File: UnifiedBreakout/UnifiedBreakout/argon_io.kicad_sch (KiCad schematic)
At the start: 3 parts, among them J14 ARGON J5

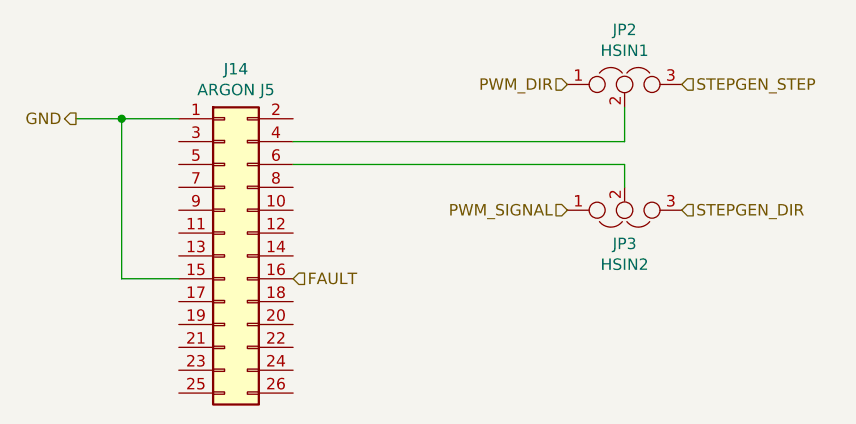
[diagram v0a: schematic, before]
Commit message: Upgrade to new KiCAD version
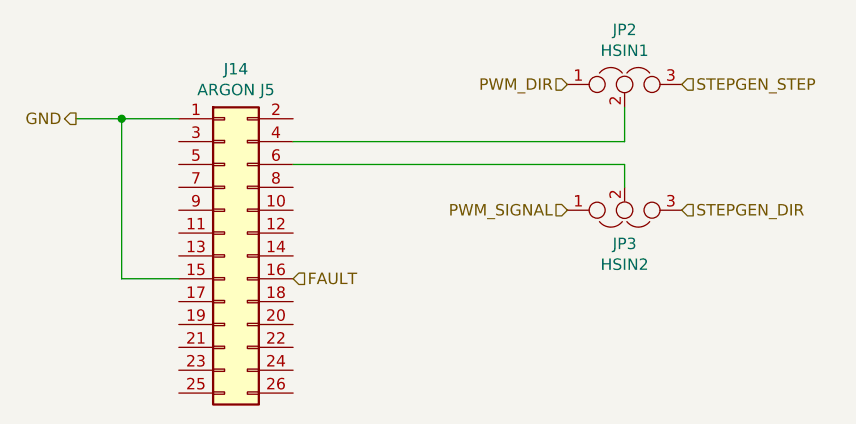
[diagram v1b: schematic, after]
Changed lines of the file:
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@@
-(kicad_sch (version 20210126) (generator eeschema)
+(kicad_sch (version 20211123) (generator eeschema)
   (paper "A4")
-  (junction (at 121.92 76.2) (diameter 0.9144) (color 0 0 0 0))
+  (junction (at 121.92 76.2) (diameter 0.9144) (color 0 0 0 0)
+  )
+  (wire (pts (xy 177.8 74.93) (xy 177.8 78.74))
+    (stroke (width 0) (type solid) (color 0 0 0 0))
+  )
   (wire (pts (xy 121.92 76.2) (xy 116.84 76.2))
     (stroke (width 0) (type solid) (color 0 0 0 0))
   )
+  (wire (pts (xy 140.97 81.28) (xy 177.8 81.28))
+    (stroke (width 0) (type solid) (color 0 0 0 0))
+  )
+  (wire (pts (xy 177.8 81.28) (xy 177.8 83.82))
+    (stroke (width 0) (type solid) (color 0 0 0 0))
+  )
   (wire (pts (xy 121.92 93.98) (xy 121.92 76.2))
+    (stroke (width 0) (type solid) (color 0 0 0 0))
+  )
+  (wire (pts (xy 140.97 78.74) (xy 177.8 78.74))
     (stroke (width 0) (type solid) (color 0 0 0 0))
   )
@@
     (stroke (width 0) (type solid) (color 0 0 0 0))
   )
-  (wire (pts (xy 140.97 78.74) (xy 177.8 78.74))
-    (stroke (width 0) (type solid) (color 0 0 0 0))
-  )
-  (wire (pts (xy 140.97 81.28) (xy 177.8 81.28))
-    (stroke (width 0) (type solid) (color 0 0 0 0))
-  )
-  (wire (pts (xy 177.8 74.93) (xy 177.8 78.74))
-    (stroke (width 0) (type solid) (color 0 0 0 0))
-  )
-  (wire (pts (xy 177.8 81.28) (xy 177.8 83.82))
-    (stroke (width 0) (type solid) (color 0 0 0 0))
-  )
   (hierarchical_label "GND" (shape output) (at 116.84 76.2 180)
-    (effects (font (size 1.27 1.27)) (justify right))
-  )
-  (hierarchical_label "FAULT" (shape input) (at 140.97 93.98 0)
-    (effects (font (size 1.27 1.27)) (justify left))
-  )
-  (hierarchical_label "PWM_DIR" (shape input) (at 171.45 72.39 180)
     (effects (font (size 1.27 1.27)) (justify right))
   )
@@
     (effects (font (size 1.27 1.27)) (justify left))
   )
-  (symbol (lib_id "UnifiedBreakout-rescue:Jumper_NC_Dual-Device") (at 177.8 72.39 0) (unit 1)
-    (in_bom yes) (on_board yes)
-    (property "Reference" "JP2" (id 0) (at 177.8 66.3194 0))
-    (property "Value" "HSIN1" (id 1) (at 177.8 68.6308 0))
-    (property "Footprint" "Connector_PinHeader_2.54mm:PinHeader_1x03_P2.54mm_Vertical" (id 2) (at 177.8 72.39 0)
-      (effects (font (size 1.27 1.27)) hide)
-    )
-    (property "Datasheet" "~" (id 3) (at 177.8 72.39 0)
-      (effects (font (size 1.27 1.27)) hide)
-    )
-    (pin "1")
-    (pin "2")
-    (pin "3")
+  (hierarchical_label "FAULT" (shape input) (at 140.97 93.98 0)
+    (effects (font (size 1.27 1.27)) (justify left))
   )
-  (symbol (lib_id "UnifiedBreakout-rescue:Jumper_NC_Dual-Device") (at 177.8 86.36 0) (mirror x) (unit 1)
-    (in_bom yes) (on_board yes)
-    (property "Reference" "JP3" (id 0) (at 177.8 90.0938 0))
-    (property "Value" "HSIN2" (id 1) (at 177.8 92.4052 0))
-    (property "Footprint" "Connector_PinHeader_2.54mm:PinHeader_1x03_P2.54mm_Vertical" (id 2) (at 177.8 86.36 0)
-      (effects (font (size 1.27 1.27)) hide)
-    )
-    (property "Datasheet" "~" (id 3) (at 177.8 86.36 0)
-      (effects (font (size 1.27 1.27)) hide)
-    )
-    (pin "1")
-    (pin "2")
-    (pin "3")
+  (hierarchical_label "PWM_DIR" (shape input) (at 171.45 72.39 180)
+    (effects (font (size 1.27 1.27)) (justify right))
   )
   (symbol (lib_id "UnifiedBreakout-rescue:Conn_02x13_Odd_Even-Connector_Generic") (at 133.35 91.44 0) (unit 1)
@@
     (pin "9")
   )
+  (symbol (lib_id "UnifiedBreakout-rescue:Jumper_NC_Dual-Device") (at 177.8 72.39 0) (unit 1)
+    (in_bom yes) (on_board yes)
+    (property "Reference" "JP2" (id 0) (at 177.8 66.3194 0))
+    (property "Value" "HSIN1" (id 1) (at 177.8 68.6308 0))
+    (property "Footprint" "Connector_PinHeader_2.54mm:PinHeader_1x03_P2.54mm_Vertical" (id 2) (at 177.8 72.39 0)
+      (effects (font (size 1.27 1.27)) hide)
+    )
+    (property "Datasheet" "~" (id 3) (at 177.8 72.39 0)
+      (effects (font (size 1.27 1.27)) hide)
+    )
+    (pin "1")
+    (pin "2")
+    (pin "3")
+  )
+  (symbol (lib_id "UnifiedBreakout-rescue:Jumper_NC_Dual-Device") (at 177.8 86.36 0) (mirror x) (unit 1)
+    (in_bom yes) (on_board yes)
+    (property "Reference" "JP3" (id 0) (at 177.8 90.0938 0))
+    (property "Value" "HSIN2" (id 1) (at 177.8 92.4052 0))
+    (property "Footprint" "Connector_PinHeader_2.54mm:PinHeader_1x03_P2.54mm_Vertical" (id 2) (at 177.8 86.36 0)
+      (effects (font (size 1.27 1.27)) hide)
+    )
+    (property "Datasheet" "~" (id 3) (at 177.8 86.36 0)
+      (effects (font (size 1.27 1.27)) hide)
+    )
+    (pin "1")
+    (pin "2")
+    (pin "3")
+  )
 )

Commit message: WIP updating breakout for electrical enclosure
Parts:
- J14: symbol UnifiedBreakout-rescue:Conn_02x13_Odd_Even-Connector_Generic -> Connector_Generic:Conn_02x13_Odd_Even
- JP2, JP3: symbol UnifiedBreakout-rescue:Jumper_NC_Dual-Device -> Jumper:Jumper_3_Open
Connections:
- no-connect marks 0 -> 21
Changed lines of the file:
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@@
-(kicad_sch (version 20211123) (generator eeschema)
+(kicad_sch (version 20230121) (generator eeschema)
   (paper "A4")
   (junction (at 121.92 76.2) (diameter 0.9144) (color 0 0 0 0)
   )
-  (wire (pts (xy 177.8 74.93) (xy 177.8 78.74))
-    (stroke (width 0) (type solid) (color 0 0 0 0))
-  )
+  (no_connect (at 140.97 106.68))
+  (no_connect (at 128.27 91.44))
+  (no_connect (at 128.27 86.36))
+  (no_connect (at 140.97 83.82))
+  (no_connect (at 128.27 99.06))
+  (no_connect (at 140.97 101.6))
+  (no_connect (at 128.27 96.52))
+  (no_connect (at 128.27 88.9))
+  (no_connect (at 140.97 91.44))
+  (no_connect (at 128.27 78.74))
+  (no_connect (at 128.27 81.28))
+  (no_connect (at 140.97 86.36))
+  (no_connect (at 128.27 104.14))
+  (no_connect (at 128.27 83.82))
+  (no_connect (at 128.27 106.68))
+  (no_connect (at 128.27 101.6))
+  (no_connect (at 140.97 88.9))
+  (no_connect (at 140.97 76.2))
+  (no_connect (at 140.97 99.06))
+  (no_connect (at 140.97 96.52))
+  (no_connect (at 140.97 104.14))
   (wire (pts (xy 121.92 76.2) (xy 116.84 76.2))
-    (stroke (width 0) (type solid) (color 0 0 0 0))
+    (stroke (width 0) (type solid))
   )
   (wire (pts (xy 140.97 81.28) (xy 177.8 81.28))
-    (stroke (width 0) (type solid) (color 0 0 0 0))
-  )
-  (wire (pts (xy 177.8 81.28) (xy 177.8 83.82))
-    (stroke (width 0) (type solid) (color 0 0 0 0))
+    (stroke (width 0) (type solid))
   )
   (wire (pts (xy 121.92 93.98) (xy 121.92 76.2))
-    (stroke (width 0) (type solid) (color 0 0 0 0))
+    (stroke (width 0) (type solid))
   )
   (wire (pts (xy 140.97 78.74) (xy 177.8 78.74))
-    (stroke (width 0) (type solid) (color 0 0 0 0))
+    (stroke (width 0) (type solid))
   )
   (wire (pts (xy 128.27 76.2) (xy 121.92 76.2))
-    (stroke (width 0) (type solid) (color 0 0 0 0))
+    (stroke (width 0) (type solid))
+  )
+  (wire (pts (xy 177.8 76.2) (xy 177.8 78.74))
+    (stroke (width 0) (type solid))
+  )
+  (wire (pts (xy 177.8 81.28) (xy 177.8 82.55))
+    (stroke (width 0) (type default))
   )
   (wire (pts (xy 128.27 93.98) (xy 121.92 93.98))
-    (stroke (width 0) (type solid) (color 0 0 0 0))
+    (stroke (width 0) (type solid))
   )
-  (hierarchical_label "GND" (shape output) (at 116.84 76.2 180)
+  (hierarchical_label "GND" (shape output) (at 116.84 76.2 180) (fields_autoplaced)
     (effects (font (size 1.27 1.27)) (justify right))
   )
-  (hierarchical_label "PWM_SIGNAL" (shape input) (at 171.45 86.36 180)
+  (hierarchical_label "PWM_SIGNAL" (shape input) (at 171.45 86.36 180) (fields_autoplaced)
     (effects (font (size 1.27 1.27)) (justify right))
   )
-  (hierarchical_label "STEPGEN_STEP" (shape input) (at 184.15 72.39 0)
+  (hierarchical_label "STEPGEN_STEP" (shape input) (at 184.15 72.39 0) (fields_autoplaced)
     (effects (font (size 1.27 1.27)) (justify left))
   )
-  (hierarchical_label "STEPGEN_DIR" (shape input) (at 184.15 86.36 0)
+  (hierarchical_label "STEPGEN_DIR" (shape input) (at 184.15 86.36 0) (fields_autoplaced)
     (effects (font (size 1.27 1.27)) (justify left))
   )
-  (hierarchical_label "FAULT" (shape input) (at 140.97 93.98 0)
+  (hierarchical_label "FAULT" (shape input) (at 140.97 93.98 0) (fields_autoplaced)
     (effects (font (size 1.27 1.27)) (justify left))
   )
-  (hierarchical_label "PWM_DIR" (shape input) (at 171.45 72.39 180)
+  (hierarchical_label "PWM_DIR" (shape input) (at 171.45 72.39 180) (fields_autoplaced)
     (effects (font (size 1.27 1.27)) (justify right))
   )
-  (symbol (lib_id "UnifiedBreakout-rescue:Conn_02x13_Odd_Even-Connector_Generic") (at 133.35 91.44 0) (unit 1)
-    (in_bom yes) (on_board yes)
-    (property "Reference" "J14" (id 0) (at 134.62 70.6882 0))
-    (property "Value" "ARGON J5" (id 1) (at 134.62 72.9996 0))
-    (property "Footprint" "Connector_IDC:IDC-Header_2x13_P2.54mm_Horizontal" (id 2) (at 133.35 91.44 0)
+  (symbol (lib_id "Connector_Generic:Conn_02x13_Odd_Even") (at 133.35 91.44 0) (unit 1)
+    (in_bom yes) (on_board yes) (dnp no)
+    (property "Reference" "J14" (at 134.62 70.6882 0)
+      (effects (font (size 1.27 1.27)))
+    )
+    (property "Value" "ARGON J5" (at 134.62 72.9996 0)
+      (effects (font (size 1.27 1.27)))
+    )
+    (property "Footprint" "Connector_IDC:IDC-Header_2x13_P2.54mm_Horizontal" (at 133.35 91.44 0)
       (effects (font (size 1.27 1.27)) hide)
     )
-    (property "Datasheet" "~" (id 3) (at 133.35 91.44 0)
+    (property "Datasheet" "~" (at 133.35 91.44 0)
       (effects (font (size 1.27 1.27)) hide)
     )
-    (property "MPN" "N2526-5002RB" (id 4) (at 133.35 91.44 0)
+    (property "MPN" "N2526-5002RB" (at 133.35 91.44 0)
       (effects (font (size 1.27 1.27)) hide)
     )
-    (property "Manufacturer" "3M" (id 5) (at 133.35 91.44 0)
+    (property "Manufacturer" "3M" (at 133.35 91.44 0)
+      (effects (font (size 1.27 1.27)) hide)
+    )
+    (property "Farnell PN" "" (at 133.35 91.44 0)
       (effects (font (size 1.27 1.27)) hide)
     )
@@
     (pin "8")
     (pin "9")
+    (instances
+      (project "UnifiedBreakout"
+        (path "/e63e39d7-6ac0-4ffd-8aa3-1841a4541b55/00000000-0000-0000-0000-00005e9eb9ea"
+          (reference "J14") (unit 1)
+        )
+      )
+    )
   )
-  (symbol (lib_id "UnifiedBreakout-rescue:Jumper_NC_Dual-Device") (at 177.8 72.39 0) (unit 1)
-    (in_bom yes) (on_board yes)
-    (property "Reference" "JP2" (id 0) (at 177.8 66.3194 0))
-    (property "Value" "HSIN1" (id 1) (at 177.8 68.6308 0))
-    (property "Footprint" "Connector_PinHeader_2.54mm:PinHeader_1x03_P2.54mm_Vertical" (id 2) (at 177.8 72.39 0)
+  (symbol (lib_id "Jumper:Jumper_3_Open") (at 177.8 72.39 0) (unit 1)
+    (in_bom yes) (on_board yes) (dnp no)
+    (property "Reference" "JP2" (at 177.8 66.3194 0)
+      (effects (font (size 1.27 1.27)))
+    )
+    (property "Value" "HSIN1" (at 177.8 68.6308 0)
+      (effects (font (size 1.27 1.27)))
+    )
+    (property "Footprint" "Connector_PinHeader_2.54mm:PinHeader_1x03_P2.54mm_Vertical" (at 177.8 72.39 0)
       (effects (font (size 1.27 1.27)) hide)
     )
-    (property "Datasheet" "~" (id 3) (at 177.8 72.39 0)
+    (property "Datasheet" "~" (at 177.8 72.39 0)
+      (effects (font (size 1.27 1.27)) hide)
+    )
+    (property "Farnell PN" "" (at 177.8 72.39 0)
       (effects (font (size 1.27 1.27)) hide)
     )
@@
     (pin "2")
     (pin "3")
+    (instances
+      (project "UnifiedBreakout"
+        (path "/e63e39d7-6ac0-4ffd-8aa3-1841a4541b55/00000000-0000-0000-0000-00005e9eb9ea"
+          (reference "JP2") (unit 1)
+        )
+      )
+    )
   )
-  (symbol (lib_id "UnifiedBreakout-rescue:Jumper_NC_Dual-Device") (at 177.8 86.36 0) (mirror x) (unit 1)
-    (in_bom yes) (on_board yes)
-    (property "Reference" "JP3" (id 0) (at 177.8 90.0938 0))
-    (property "Value" "HSIN2" (id 1) (at 177.8 92.4052 0))
-    (property "Footprint" "Connector_PinHeader_2.54mm:PinHeader_1x03_P2.54mm_Vertical" (id 2) (at 177.8 86.36 0)
+  (symbol (lib_id "Jumper:Jumper_3_Open") (at 177.8 86.36 0) (mirror x) (unit 1)
+    (in_bom yes) (on_board yes) (dnp no)
+    (property "Reference" "JP3" (at 177.8 90.0938 0)
+      (effects (font (size 1.27 1.27)))
+    )
+    (property "Value" "HSIN2" (at 177.8 92.4052 0)
+      (effects (font (size 1.27 1.27)))
+    )
+    (property "Footprint" "Connector_PinHeader_2.54mm:PinHeader_1x03_P2.54mm_Vertical" (at 177.8 86.36 0)
       (effects (font (size 1.27 1.27)) hide)
     )
-    (property "Datasheet" "~" (id 3) (at 177.8 86.36 0)
+    (property "Datasheet" "~" (at 177.8 86.36 0)
+      (effects (font (size 1.27 1.27)) hide)
+    )
+    (property "Farnell PN" "" (at 177.8 86.36 0)
       (effects (font (size 1.27 1.27)) hide)
     )
@@
     (pin "2")
     (pin "3")
+    (instances
+      (project "UnifiedBreakout"
+        (path "/e63e39d7-6ac0-4ffd-8aa3-1841a4541b55/00000000-0000-0000-0000-00005e9eb9ea"
+          (reference "JP3") (unit 1)
+        )
+      )
+    )
   )
 )

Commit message: Add dual level DB25
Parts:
- J14: footprint Connector_IDC:IDC-Header_2x13_P2.54mm_Horizontal -> Connector_IDC:IDC-Header_2x13_P2.54mm_Vertical; Farnell PN (none) -> 1642022; MPN N2526-5002RB -> 61202621621; Manufacturer 3M -> WURTH ELECTRONIK
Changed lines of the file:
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@@
       (effects (font (size 1.27 1.27)))
     )
-    (property "Footprint" "Connector_IDC:IDC-Header_2x13_P2.54mm_Horizontal" (at 133.35 91.44 0)
+    (property "Footprint" "Connector_IDC:IDC-Header_2x13_P2.54mm_Vertical" (at 133.35 91.44 0)
       (effects (font (size 1.27 1.27)) hide)
     )
@@
       (effects (font (size 1.27 1.27)) hide)
     )
-    (property "MPN" "N2526-5002RB" (at 133.35 91.44 0)
+    (property "MPN" "61202621621" (at 133.35 91.44 0)
       (effects (font (size 1.27 1.27)) hide)
     )
-    (property "Manufacturer" "3M" (at 133.35 91.44 0)
+    (property "Manufacturer" "WURTH ELECTRONIK" (at 133.35 91.44 0)
       (effects (font (size 1.27 1.27)) hide)
     )
-    (property "Farnell PN" "" (at 133.35 91.44 0)
+    (property "Farnell PN" "1642022" (at 133.35 91.44 0)
       (effects (font (size 1.27 1.27)) hide)
     )

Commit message: Update IO and opto
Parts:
- renumbered J14 to J2, JP2 to JP1, JP3 to JP2
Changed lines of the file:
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@@
   (symbol (lib_id "Connector_Generic:Conn_02x13_Odd_Even") (at 133.35 91.44 0) (unit 1)
     (in_bom yes) (on_board yes) (dnp no)
-    (property "Reference" "J14" (at 134.62 70.6882 0)
+    (property "Reference" "J2" (at 134.62 70.6882 0)
       (effects (font (size 1.27 1.27)))
     )
@@
       (project "UnifiedBreakout"
         (path "/e63e39d7-6ac0-4ffd-8aa3-1841a4541b55/00000000-0000-0000-0000-00005e9eb9ea"
-          (reference "J14") (unit 1)
+          (reference "J2") (unit 1)
         )
       )
@@
   (symbol (lib_id "Jumper:Jumper_3_Open") (at 177.8 72.39 0) (unit 1)
     (in_bom yes) (on_board yes) (dnp no)
-    (property "Reference" "JP2" (at 177.8 66.3194 0)
+    (property "Reference" "JP1" (at 177.8 66.3194 0)
       (effects (font (size 1.27 1.27)))
     )
@@
       (project "UnifiedBreakout"
         (path "/e63e39d7-6ac0-4ffd-8aa3-1841a4541b55/00000000-0000-0000-0000-00005e9eb9ea"
-          (reference "JP2") (unit 1)
+          (reference "JP1") (unit 1)
         )
       )
@@
   (symbol (lib_id "Jumper:Jumper_3_Open") (at 177.8 86.36 0) (mirror x) (unit 1)
     (in_bom yes) (on_board yes) (dnp no)
-    (property "Reference" "JP3" (at 177.8 90.0938 0)
+    (property "Reference" "JP2" (at 177.8 90.0938 0)
       (effects (font (size 1.27 1.27)))
     )
@@
       (project "UnifiedBreakout"
         (path "/e63e39d7-6ac0-4ffd-8aa3-1841a4541b55/00000000-0000-0000-0000-00005e9eb9ea"
-          (reference "JP3") (unit 1)
+          (reference "JP2") (unit 1)
         )
       )

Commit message: Started some layout
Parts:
- J2: now left out of the parts list
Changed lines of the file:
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@@
   )
   (symbol (lib_id "Connector_Generic:Conn_02x13_Odd_Even") (at 133.35 91.44 0) (unit 1)
-    (in_bom yes) (on_board yes) (dnp no)
+    (in_bom no) (on_board yes) (dnp no)
     (property "Reference" "J2" (at 134.62 70.6882 0)
       (effects (font (size 1.27 1.27)))

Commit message: Some layout
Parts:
- renumbered J2 to J3
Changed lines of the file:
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@@
   (symbol (lib_id "Connector_Generic:Conn_02x13_Odd_Even") (at 133.35 91.44 0) (unit 1)
     (in_bom no) (on_board yes) (dnp no)
-    (property "Reference" "J2" (at 134.62 70.6882 0)
+    (property "Reference" "J3" (at 134.62 70.6882 0)
       (effects (font (size 1.27 1.27)))
     )
@@
       (project "UnifiedBreakout"
         (path "/e63e39d7-6ac0-4ffd-8aa3-1841a4541b55/00000000-0000-0000-0000-00005e9eb9ea"
-          (reference "J2") (unit 1)
+          (reference "J3") (unit 1)
         )
       )

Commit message: Final tweaks for production
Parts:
- removed JP1: HSIN1, Connector_PinHeader_2.54mm:PinHeader_1x03_P2.54mm_Vertical, symbol Jumper:Jumper_3_Open
- removed JP2: HSIN2, Connector_PinHeader_2.54mm:PinHeader_1x03_P2.54mm_Vertical, symbol Jumper:Jumper_3_Open
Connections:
- no-connect marks 21 -> 23
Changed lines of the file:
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@@
   )
   (no_connect (at 140.97 106.68))
+  (no_connect (at 140.97 81.28))
   (no_connect (at 128.27 91.44))
   (no_connect (at 128.27 86.36))
   (no_connect (at 140.97 83.82))
   (no_connect (at 128.27 99.06))
+  (no_connect (at 140.97 78.74))
   (no_connect (at 140.97 101.6))
   (no_connect (at 128.27 96.52))
@@
     (stroke (width 0) (type solid))
   )
-  (wire (pts (xy 140.97 81.28) (xy 177.8 81.28))
-    (stroke (width 0) (type solid))
-  )
   (wire (pts (xy 121.92 93.98) (xy 121.92 76.2))
-    (stroke (width 0) (type solid))
-  )
-  (wire (pts (xy 140.97 78.74) (xy 177.8 78.74))
     (stroke (width 0) (type solid))
   )
   (wire (pts (xy 128.27 76.2) (xy 121.92 76.2))
     (stroke (width 0) (type solid))
-  )
-  (wire (pts (xy 177.8 76.2) (xy 177.8 78.74))
-    (stroke (width 0) (type solid))
-  )
-  (wire (pts (xy 177.8 81.28) (xy 177.8 82.55))
-    (stroke (width 0) (type default))
   )
   (wire (pts (xy 128.27 93.98) (xy 121.92 93.98))
@@
     (effects (font (size 1.27 1.27)) (justify right))
   )
-  (hierarchical_label "PWM_SIGNAL" (shape input) (at 171.45 86.36 180) (fields_autoplaced)
-    (effects (font (size 1.27 1.27)) (justify right))
-  )
-  (hierarchical_label "STEPGEN_STEP" (shape input) (at 184.15 72.39 0) (fields_autoplaced)
-    (effects (font (size 1.27 1.27)) (justify left))
-  )
-  (hierarchical_label "STEPGEN_DIR" (shape input) (at 184.15 86.36 0) (fields_autoplaced)
-    (effects (font (size 1.27 1.27)) (justify left))
-  )
   (hierarchical_label "FAULT" (shape input) (at 140.97 93.98 0) (fields_autoplaced)
     (effects (font (size 1.27 1.27)) (justify left))
-  )
-  (hierarchical_label "PWM_DIR" (shape input) (at 171.45 72.39 180) (fields_autoplaced)
-    (effects (font (size 1.27 1.27)) (justify right))
   )
   (symbol (lib_id "Connector_Generic:Conn_02x13_Odd_Even") (at 133.35 91.44 0) (unit 1)
@@
         )
       )
-    )
-  )
-  (symbol (lib_id "Jumper:Jumper_3_Open") (at 177.8 72.39 0) (unit 1)
-    (in_bom yes) (on_board yes) (dnp no)
-    (property "Reference" "JP1" (at 177.8 66.3194 0)
-      (effects (font (size 1.27 1.27)))
-    )
-    (property "Value" "HSIN1" (at 177.8 68.6308 0)
-      (effects (font (size 1.27 1.27)))
-    )
-    (property "Footprint" "Connector_PinHeader_2.54mm:PinHeader_1x03_P2.54mm_Vertical" (at 177.8 72.39 0)
-      (effects (font (size 1.27 1.27)) hide)
-    )
-    (property "Datasheet" "~" (at 177.8 72.39 0)
-      (effects (font (size 1.27 1.27)) hide)
-    )
-    (property "Farnell PN" "" (at 177.8 72.39 0)
-      (effects (font (size 1.27 1.27)) hide)
-    )
-    (pin "1")
-    (pin "2")
-    (pin "3")
-    (instances
-      (project "UnifiedBreakout"
-        (path "/e63e39d7-6ac0-4ffd-8aa3-1841a4541b55/00000000-0000-0000-0000-00005e9eb9ea"
-          (reference "JP1") (unit 1)
-        )
-      )
-    )
-  )
-  (symbol (lib_id "Jumper:Jumper_3_Open") (at 177.8 86.36 0) (mirror x) (unit 1)
-    (in_bom yes) (on_board yes) (dnp no)
-    (property "Reference" "JP2" (at 177.8 90.0938 0)
-      (effects (font (size 1.27 1.27)))
-    )
-    (property "Value" "HSIN2" (at 177.8 92.4052 0)
-      (effects (font (size 1.27 1.27)))
-    )
-    (property "Footprint" "Connector_PinHeader_2.54mm:PinHeader_1x03_P2.54mm_Vertical" (at 177.8 86.36 0)
-      (effects (font (size 1.27 1.27)) hide)
-    )
-    (property "Datasheet" "~" (at 177.8 86.36 0)
-      (effects (font (size 1.27 1.27)) hide)
-    )
-    (property "Farnell PN" "" (at 177.8 86.36 0)
-      (effects (font (size 1.27 1.27)) hide)
-    )
-    (pin "1")
-    (pin "2")
-    (pin "3")
-    (instances
-      (project "UnifiedBreakout"
-        (path "/e63e39d7-6ac0-4ffd-8aa3-1841a4541b55/00000000-0000-0000-0000-00005e9eb9ea"
-          (reference "JP2") (unit 1)
-        )
-      )

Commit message: v3.1
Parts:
- J3: now in the parts list
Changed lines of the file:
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@@
   )
   (symbol (lib_id "Connector_Generic:Conn_02x13_Odd_Even") (at 133.35 91.44 0) (unit 1)
-    (in_bom no) (on_board yes) (dnp no)
+    (in_bom yes) (on_board yes) (dnp no)
     (property "Reference" "J3" (at 134.62 70.6882 0)
       (effects (font (size 1.27 1.27)))
